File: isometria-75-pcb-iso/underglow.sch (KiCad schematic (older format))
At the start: 36 parts, among them U301 74LVC1G125

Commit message: final touches
changed some 0603 to 0402 for consistency, added vias to properly better ground planes, added LCSC part numbers for jlcpcb assembly
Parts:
- C301, C302, C303, C304, C305, C306, C307, C308, C309, C310, C311, C312, C313, C314, C315, C316, C317, C318: LCSC (none) -> C1525
- D301, D302, D303, D304, D305, D306, D307, D308, D309, D310, D311, D312, D313, D314, D315, D316, D317: LCSC (none) -> /
- U301: LCSC (none) -> C23654
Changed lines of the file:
@@
 F 2 "Capacitor_SMD:C_0402_1005Metric" H 3000 1650 50  0001 C CNN
 F 3 "~" H 3000 1650 50  0001 C CNN
+F 4 "C1525" H 3000 1650 50  0001 C CNN "LCSC"
 	1    3000 1650
 	1    0    0    -1
@@
 F 2 "LED_SMD:LED_SK6812MINI_PLCC4_3.5x3.5mm_P1.75mm" H 2700 1150 50  0001 L TNN
 F 3 "https://cdn-shop.adafruit.com/product-files/2686/SK6812MINI_REV.01-1-2.pdf" H 2750 1075 50  0001 L TNN
+F 4 "/" H 2650 1450 50  0001 C CNN "LCSC"
 	1    2650 1450
 	1    0    0    -1
@@
 F 2 "Capacitor_SMD:C_0402_1005Metric" H 3850 1650 50  0001 C CNN
 F 3 "~" H 3850 1650 50  0001 C CNN
+F 4 "C1525" H 3850 1650 50  0001 C CNN "LCSC"
 	1    3850 1650
 	1    0    0    -1
@@
 F 2 "LED_SMD:LED_SK6812MINI_PLCC4_3.5x3.5mm_P1.75mm" H 3550 1150 50  0001 L TNN
 F 3 "https://cdn-shop.adafruit.com/product-files/2686/SK6812MINI_REV.01-1-2.pdf" H 3600 1075 50  0001 L TNN
+F 4 "/" H 3500 1450 50  0001 C CNN "LCSC"
 	1    3500 1450
 	1    0    0    -1
@@
 F 2 "Capacitor_SMD:C_0402_1005Metric" H 4700 1650 50  0001 C CNN
 F 3 "~" H 4700 1650 50  0001 C CNN
+F 4 "C1525" H 4700 1650 50  0001 C CNN "LCSC"
 	1    4700 1650
 	1    0    0    -1
@@
 F 2 "LED_SMD:LED_SK6812MINI_PLCC4_3.5x3.5mm_P1.75mm" H 4400 1150 50  0001 L TNN
 F 3 "https://cdn-shop.adafruit.com/product-files/2686/SK6812MINI_REV.01-1-2.pdf" H 4450 1075 50  0001 L TNN
+F 4 "/" H 4350 1450 50  0001 C CNN "LCSC"
 	1    4350 1450
 	1    0    0    -1
@@
 F 2 "Capacitor_SMD:C_0402_1005Metric" H 5550 1650 50  0001 C CNN
 F 3 "~" H 5550 1650 50  0001 C CNN
+F 4 "C1525" H 5550 1650 50  0001 C CNN "LCSC"
 	1    5550 1650
 	1    0    0    -1
@@
 F 2 "LED_SMD:LED_SK6812MINI_PLCC4_3.5x3.5mm_P1.75mm" H 5250 1150 50  0001 L TNN
 F 3 "https://cdn-shop.adafruit.com/product-files/2686/SK6812MINI_REV.01-1-2.pdf" H 5300 1075 50  0001 L TNN
+F 4 "/" H 5200 1450 50  0001 C CNN "LCSC"
 	1    5200 1450
 	1    0    0    -1
@@
 F 2 "Capacitor_SMD:C_0402_1005Metric" H 7200 1650 50  0001 C CNN
 F 3 "~" H 7200 1650 50  0001 C CNN
+F 4 "C1525" H 7200 1650 50  0001 C CNN "LCSC"
 	1    7200 1650
 	1    0    0    -1
@@
 F 2 "LED_SMD:LED_SK6812MINI_PLCC4_3.5x3.5mm_P1.75mm" H 6900 1150 50  0001 L TNN
 F 3 "https://cdn-shop.adafruit.com/product-files/2686/SK6812MINI_REV.01-1-2.pdf" H 6950 1075 50  0001 L TNN
+F 4 "/" H 6850 1450 50  0001 C CNN "LCSC"
 	1    6850 1450
 	1    0    0    -1
@@
 F 2 "Capacitor_SMD:C_0402_1005Metric" H 8050 1650 50  0001 C CNN
 F 3 "~" H 8050 1650 50  0001 C CNN
+F 4 "C1525" H 8050 1650 50  0001 C CNN "LCSC"
 	1    8050 1650
 	1    0    0    -1
@@
 F 2 "LED_SMD:LED_SK6812MINI_PLCC4_3.5x3.5mm_P1.75mm" H 7750 1150 50  0001 L TNN
 F 3 "https://cdn-shop.adafruit.com/product-files/2686/SK6812MINI_REV.01-1-2.pdf" H 7800 1075 50  0001 L TNN
+F 4 "/" H 7700 1450 50  0001 C CNN "LCSC"
 	1    7700 1450
 	1    0    0    -1
@@
 F 2 "Capacitor_SMD:C_0402_1005Metric" H 8900 1650 50  0001 C CNN
 F 3 "~" H 8900 1650 50  0001 C CNN
+F 4 "C1525" H 8900 1650 50  0001 C CNN "LCSC"
 	1    8900 1650
 	1    0    0    -1
@@
 F 2 "LED_SMD:LED_SK6812MINI_PLCC4_3.5x3.5mm_P1.75mm" H 8600 1150 50  0001 L TNN
 F 3 "https://cdn-shop.adafruit.com/product-files/2686/SK6812MINI_REV.01-1-2.pdf" H 8650 1075 50  0001 L TNN
+F 4 "/" H 8550 1450 50  0001 C CNN "LCSC"
 	1    8550 1450
 	1    0    0    -1
@@
 F 2 "Capacitor_SMD:C_0402_1005Metric" H 9750 1650 50  0001 C CNN
 F 3 "~" H 9750 1650 50  0001 C CNN
+F 4 "C1525" H 9750 1650 50  0001 C CNN "LCSC"
 	1    9750 1650
 	1    0    0    -1
@@
 F 2 "LED_SMD:LED_SK6812MINI_PLCC4_3.5x3.5mm_P1.75mm" H 9450 1150 50  0001 L TNN
 F 3 "https://cdn-shop.adafruit.com/product-files/2686/SK6812MINI_REV.01-1-2.pdf" H 9500 1075 50  0001 L TNN
+F 4 "/" H 9400 1450 50  0001 C CNN "LCSC"
 	1    9400 1450
 	1    0    0    -1
@@
 F 2 "Capacitor_SMD:C_0402_1005Metric" H 3000 2800 50  0001 C CNN
 F 3 "~" H 3000 2800 50  0001 C CNN
+F 4 "C1525" H 3000 2800 50  0001 C CNN "LCSC"
 	1    3000 2800
 	1    0    0    -1
@@
 F 2 "LED_SMD:LED_SK6812MINI_PLCC4_3.5x3.5mm_P1.75mm" H 2700 2300 50  0001 L TNN
 F 3 "https://cdn-shop.adafruit.com/product-files/2686/SK6812MINI_REV.01-1-2.pdf" H 2750 2225 50  0001 L TNN
+F 4 "/" H 2650 2600 50  0001 C CNN "LCSC"
 	1    2650 2600
 	1    0    0    -1
@@
 F 2 "Capacitor_SMD:C_0402_1005Metric" H 3850 2800 50  0001 C CNN
 F 3 "~" H 3850 2800 50  0001 C CNN
+F 4 "C1525" H 3850 2800 50  0001 C CNN "LCSC"
 	1    3850 2800
 	1    0    0    -1
@@
 F 2 "LED_SMD:LED_SK6812MINI_PLCC4_3.5x3.5mm_P1.75mm" H 3550 2300 50  0001 L TNN
 F 3 "https://cdn-shop.adafruit.com/product-files/2686/SK6812MINI_REV.01-1-2.pdf" H 3600 2225 50  0001 L TNN
+F 4 "/" H 3500 2600 50  0001 C CNN "LCSC"
 	1    3500 2600
 	1    0    0    -1
@@
 F 2 "Package_TO_SOT_SMD:SOT-23-5" H 1650 1450 50  0001 C CNN
 F 3 "http://www.ti.com/lit/sg/scyt129e/scyt129e.pdf" H 1650 1450 50  0001 C CNN
+F 4 "C23654" H 1650 1450 50  0001 C CNN "LCSC"
 	1    1650 1450
 	1    0    0    -1
@@
 F 2 "Capacitor_SMD:C_0402_1005Metric" H 1950 1650 50  0001 C CNN
 F 3 "~" H 1950 1650 50  0001 C CNN
+F 4 "C1525" H 1950 1650 50  0001 C CNN "LCSC"
 	1    1950 1650
 	1    0    0    -1
@@
 F 2 "Capacitor_SMD:C_0402_1005Metric" H 4700 2800 50  0001 C CNN
 F 3 "~" H 4700 2800 50  0001 C CNN
+F 4 "C1525" H 4700 2800 50  0001 C CNN "LCSC"
 	1    4700 2800
 	1    0    0    -1
@@
 F 2 "LED_SMD:LED_SK6812MINI_PLCC4_3.5x3.5mm_P1.75mm" H 4400 2300 50  0001 L TNN
 F 3 "https://cdn-shop.adafruit.com/product-files/2686/SK6812MINI_REV.01-1-2.pdf" H 4450 2225 50  0001 L TNN
+F 4 "/" H 4350 2600 50  0001 C CNN "LCSC"
 	1    4350 2600
 	1    0    0    -1
@@
 F 2 "Capacitor_SMD:C_0402_1005Metric" H 5550 2800 50  0001 C CNN
 F 3 "~" H 5550 2800 50  0001 C CNN
+F 4 "C1525" H 5550 2800 50  0001 C CNN "LCSC"
 	1    5550 2800
 	1    0    0    -1
@@
 F 2 "LED_SMD:LED_SK6812MINI_PLCC4_3.5x3.5mm_P1.75mm" H 5250 2300 50  0001 L TNN
 F 3 "https://cdn-shop.adafruit.com/product-files/2686/SK6812MINI_REV.01-1-2.pdf" H 5300 2225 50  0001 L TNN
+F 4 "/" H 5200 2600 50  0001 C CNN "LCSC"
 	1    5200 2600
 	1    0    0    -1
@@
 F 2 "Capacitor_SMD:C_0402_1005Metric" H 6400 2800 50  0001 C CNN
 F 3 "~" H 6400 2800 50  0001 C CNN
+F 4 "C1525" H 6400 2800 50  0001 C CNN "LCSC"
 	1    6400 2800
 	1    0    0    -1
@@
 F 2 "LED_SMD:LED_SK6812MINI_PLCC4_3.5x3.5mm_P1.75mm" H 6100 2300 50  0001 L TNN
 F 3 "https://cdn-shop.adafruit.com/product-files/2686/SK6812MINI_REV.01-1-2.pdf" H 6150 2225 50  0001 L TNN
+F 4 "/" H 6050 2600 50  0001 C CNN "LCSC"
 	1    6050 2600
 	1    0    0    -1
@@
 F 2 "Capacitor_SMD:C_0402_1005Metric" H 7250 2800 50  0001 C CNN
 F 3 "~" H 7250 2800 50  0001 C CNN
+F 4 "C1525" H 7250 2800 50  0001 C CNN "LCSC"
 	1    7250 2800
 	1    0    0    -1
@@
 F 2 "LED_SMD:LED_SK6812MINI_PLCC4_3.5x3.5mm_P1.75mm" H 6950 2300 50  0001 L TNN
 F 3 "https://cdn-shop.adafruit.com/product-files/2686/SK6812MINI_REV.01-1-2.pdf" H 7000 2225 50  0001 L TNN
+F 4 "/" H 6900 2600 50  0001 C CNN "LCSC"
 	1    6900 2600
 	1    0    0    -1
@@
 F 2 "Capacitor_SMD:C_0402_1005Metric" H 8100 2800 50  0001 C CNN
 F 3 "~" H 8100 2800 50  0001 C CNN
+F 4 "C1525" H 8100 2800 50  0001 C CNN "LCSC"
 	1    8100 2800
 	1    0    0    -1
@@
 F 2 "LED_SMD:LED_SK6812MINI_PLCC4_3.5x3.5mm_P1.75mm" H 7800 2300 50  0001 L TNN
 F 3 "https://cdn-shop.adafruit.com/product-files/2686/SK6812MINI_REV.01-1-2.pdf" H 7850 2225 50  0001 L TNN
+F 4 "/" H 7750 2600 50  0001 C CNN "LCSC"
 	1    7750 2600
 	1    0    0    -1
@@
 F 2 "Capacitor_SMD:C_0402_1005Metric" H 8950 2800 50  0001 C CNN
 F 3 "~" H 8950 2800 50  0001 C CNN
+F 4 "C1525" H 8950 2800 50  0001 C CNN "LCSC"
 	1    8950 2800
 	1    0    0    -1
@@
 F 2 "LED_SMD:LED_SK6812MINI_PLCC4_3.5x3.5mm_P1.75mm" H 8650 2300 50  0001 L TNN
 F 3 "https://cdn-shop.adafruit.com/product-files/2686/SK6812MINI_REV.01-1-2.pdf" H 8700 2225 50  0001 L TNN
+F 4 "/" H 8600 2600 50  0001 C CNN "LCSC"
 	1    8600 2600
 	1    0    0    -1
@@
 F 2 "Capacitor_SMD:C_0402_1005Metric" H 6400 1650 50  0001 C CNN
 F 3 "~" H 6400 1650 50  0001 C CNN
+F 4 "C1525" H 6400 1650 50  0001 C CNN "LCSC"
 	1    6400 1650
 	1    0    0    -1
@@
 F 2 "LED_SMD:LED_SK6812MINI_PLCC4_3.5x3.5mm_P1.75mm" H 6100 1150 50  0001 L TNN
 F 3 "https://cdn-shop.adafruit.com/product-files/2686/SK6812MINI_REV.01-1-2.pdf" H 6150 1075 50  0001 L TNN
+F 4 "/" H 6050 1450 50  0001 C CNN "LCSC"
 	1    6050 1450
 	1    0    0    -1

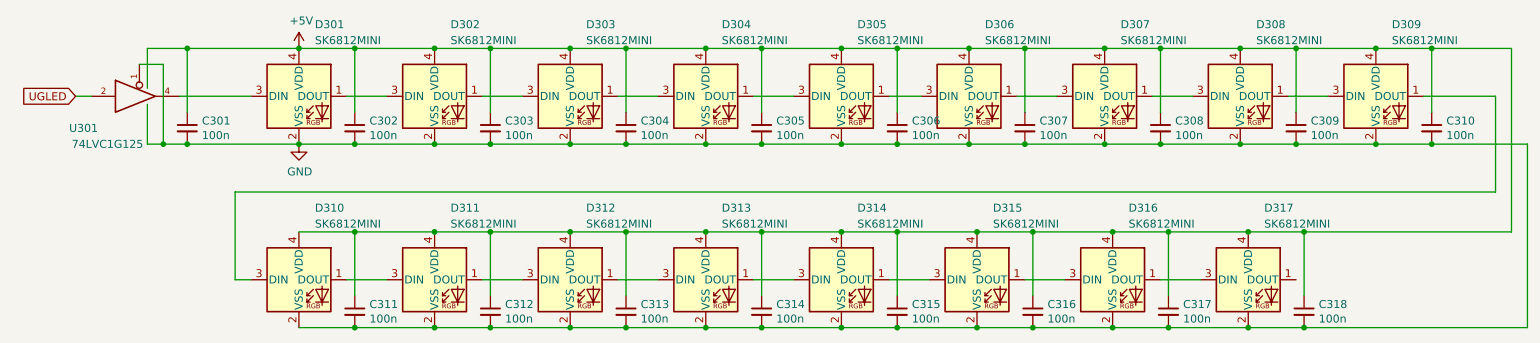
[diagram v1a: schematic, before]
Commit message: improved componend value formatting
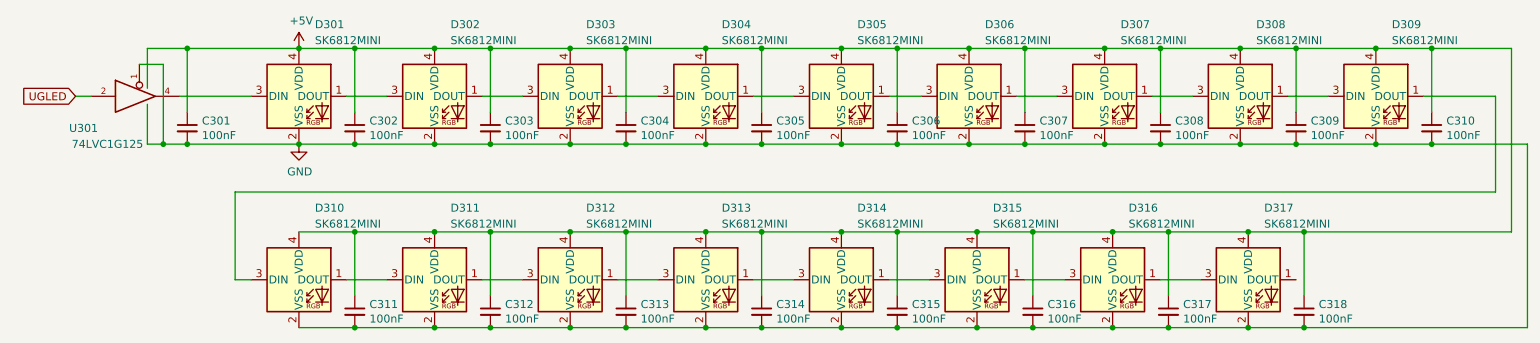
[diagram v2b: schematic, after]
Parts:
- C301, C302, C303, C304, C305, C306, C307, C308, C309, C310, C311, C312, C313, C314, C315, C316, C317, C318: value 100n -> 100nF
- D301, D302, D303, D304, D305, D306, D307, D308, D309, D310, D311, D312, D313, D314, D315, D316, D317: LCSC / -> (none)

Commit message: fixed minor bugs, migrated to new libs
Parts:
- renumbered C301 to C20, C302 to C21, C303 to C22, C304 to C23, C305 to C24, C306 to C25, C307 to C26, C308 to C27, C309 to C28, C310 to C29, C311 to C30, C312 to C31, C313 to C32, C314 to C33, C315 to C34, C316 to C35, C317 to C36, C318 to C37, D317 to D100, D301 to D84, D302 to D85, D303 to D86, D304 to D87, D305 to D88, D306 to D89, D307 to D90, D308 to D91, D309 to D92, D310 to D93, D311 to D94, D312 to D95, D313 to D96, D314 to D97, D315 to D98, D316 to D99, U301 to U3

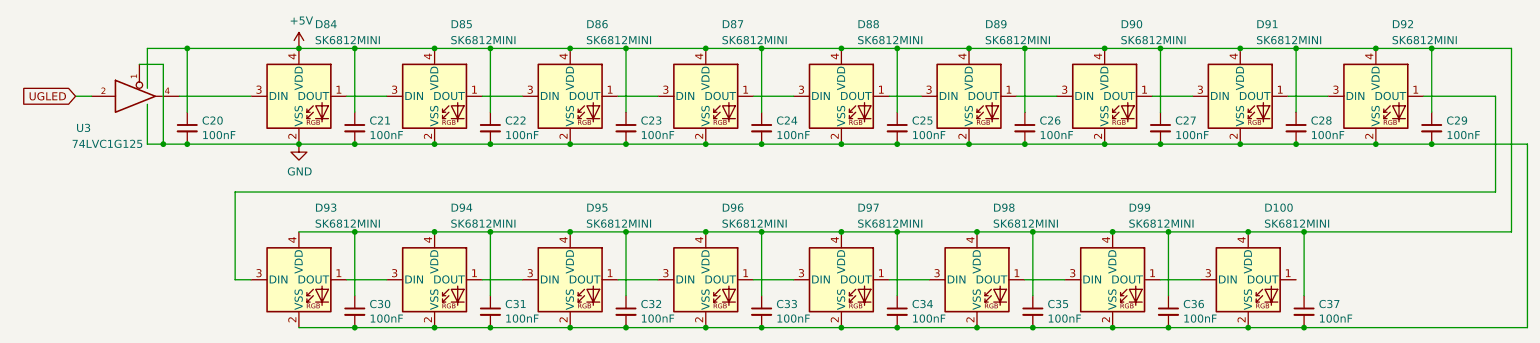
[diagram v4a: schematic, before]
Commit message: started nRF v2 rework
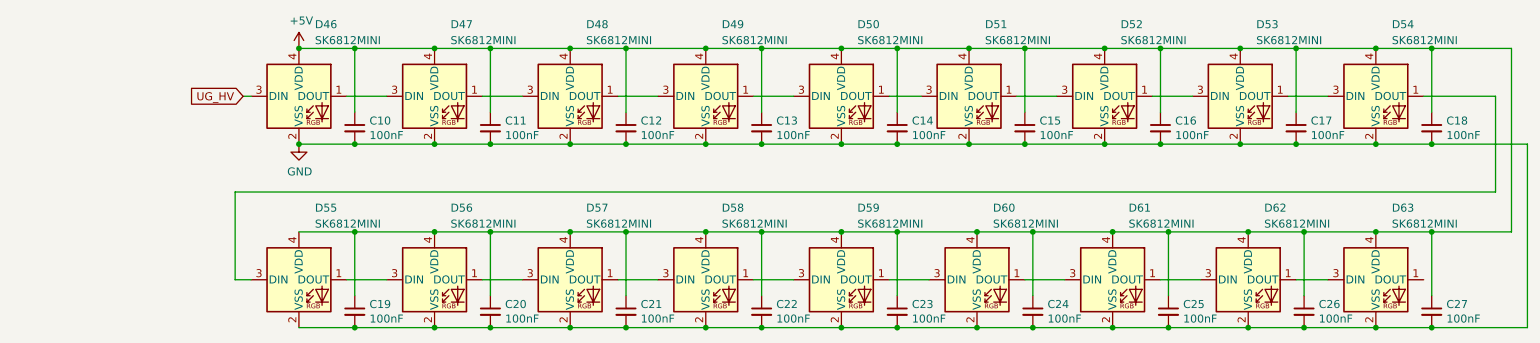
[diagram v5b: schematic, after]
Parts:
- removed C20: 100nF, Capacitor_SMD:C_0402_1005Metric, symbol Device:C_Small
- removed U3: 74LVC1G125, Package_TO_SOT_SMD:SOT-23-5, symbol 74xGxx:74LVC1G125
- added C27: 100nF, Capacitor_SMD:C_0603_1608Metric_Pad1.05x0.95mm_HandSolder, symbol Device:C_Small
- added D63: SK6812MINI, LED_SMD:LED_SK6812MINI_PLCC4_3.5x3.5mm_P1.75mm, symbol LED:SK6812MINI
- C10: renamed from C21; footprint Capacitor_SMD:C_0402_1005Metric -> Capacitor_SMD:C_0603_1608Metric_Pad1.05x0.95mm_HandSolder
- C11: renamed from C22; footprint Capacitor_SMD:C_0402_1005Metric -> Capacitor_SMD:C_0603_1608Metric_Pad1.05x0.95mm_HandSolder
- C12: renamed from C23; footprint Capacitor_SMD:C_0402_1005Metric -> Capacitor_SMD:C_0603_1608Metric_Pad1.05x0.95mm_HandSolder
- C13: renamed from C24; footprint Capacitor_SMD:C_0402_1005Metric -> Capacitor_SMD:C_0603_1608Metric_Pad1.05x0.95mm_HandSolder
- C14: renamed from C25; footprint Capacitor_SMD:C_0402_1005Metric -> Capacitor_SMD:C_0603_1608Metric_Pad1.05x0.95mm_HandSolder
- C15: renamed from C26; footprint Capacitor_SMD:C_0402_1005Metric -> Capacitor_SMD:C_0603_1608Metric_Pad1.05x0.95mm_HandSolder
- C16: renamed from C27; footprint Capacitor_SMD:C_0402_1005Metric -> Capacitor_SMD:C_0603_1608Metric_Pad1.05x0.95mm_HandSolder
- C17: renamed from C28; footprint Capacitor_SMD:C_0402_1005Metric -> Capacitor_SMD:C_0603_1608Metric_Pad1.05x0.95mm_HandSolder
- C18: renamed from C29; footprint Capacitor_SMD:C_0402_1005Metric -> Capacitor_SMD:C_0603_1608Metric_Pad1.05x0.95mm_HandSolder
- C19: renamed from C30; footprint Capacitor_SMD:C_0402_1005Metric -> Capacitor_SMD:C_0603_1608Metric_Pad1.05x0.95mm_HandSolder
- C20: renamed from C31; footprint Capacitor_SMD:C_0402_1005Metric -> Capacitor_SMD:C_0603_1608Metric_Pad1.05x0.95mm_HandSolder
- C21: renamed from C32; footprint Capacitor_SMD:C_0402_1005Metric -> Capacitor_SMD:C_0603_1608Metric_Pad1.05x0.95mm_HandSolder
- C22: renamed from C33; footprint Capacitor_SMD:C_0402_1005Metric -> Capacitor_SMD:C_0603_1608Metric_Pad1.05x0.95mm_HandSolder
- C23: renamed from C34; footprint Capacitor_SMD:C_0402_1005Metric -> Capacitor_SMD:C_0603_1608Metric_Pad1.05x0.95mm_HandSolder
- C24: renamed from C35; footprint Capacitor_SMD:C_0402_1005Metric -> Capacitor_SMD:C_0603_1608Metric_Pad1.05x0.95mm_HandSolder
- C25: renamed from C36; footprint Capacitor_SMD:C_0402_1005Metric -> Capacitor_SMD:C_0603_1608Metric_Pad1.05x0.95mm_HandSolder
- C26: renamed from C37; footprint Capacitor_SMD:C_0402_1005Metric -> Capacitor_SMD:C_0603_1608Metric_Pad1.05x0.95mm_HandSolder
- renumbered D84 to D46, D85 to D47, D86 to D48, D87 to D49, D88 to D50, D89 to D51, D90 to D52, D91 to D53, D92 to D54, D93 to D55, D94 to D56, D95 to D57, D96 to D58, D97 to D59, D98 to D60, D99 to D61, D100 to D62
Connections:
- net +5V: now also C27.1, D63.4 (VDD)
- net GND: now also C27.2, D63.2 (VSS)
- net UG_HV: now reaches D46.3 (DIN)
- net at D62.1 (DOUT): now also D63.3 (DIN)

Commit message: began renaming project
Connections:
- net +5V renamed UG_PWR
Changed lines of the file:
@@
 	2950 2600 3200 2600
 $Comp
-L power:GND #PWR019
+L power:GND #PWR023
 U 1 1 5E718AF7
 P 2650 1750
-F 0 "#PWR019" H 2650 1500 50  0001 C CNN
+F 0 "#PWR023" H 2650 1500 50  0001 C CNN
 F 1 "GND" H 2655 1577 50  0000 C CNN
 F 2 "" H 2650 1750 50  0001 C CNN
@@
 $EndComp
 Connection ~ 2650 1750
-$Comp
-L power:+5V #PWR018
-U 1 1 5E71981C
-P 2650 1150
-F 0 "#PWR018" H 2650 1000 50  0001 C CNN
-F 1 "+5V" H 2665 1323 50  0000 C CNN
-F 2 "" H 2650 1150 50  0001 C CNN
-F 3 "" H 2650 1150 50  0001 C CNN
-	1    2650 1150
-	1    0    0    -1
-$EndComp
-Connection ~ 2650 1150
 Text GLabel 2300 1450 0    50   Input ~ 0
 UG_HV
@@
 Wire Wire Line
 	2350 1450 2300 1450
+Text GLabel 2300 1150 0    50   Input ~ 0
+UG_PWR
+Wire Wire Line
+	2300 1150 2650 1150
+Connection ~ 2650 1150
 $EndSCHEMATC
